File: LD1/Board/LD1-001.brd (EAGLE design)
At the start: 72 x 72 mm, 13 parts, among them IC1 TLC5941NT, IC2 TLC5941NT, IC3 TLC5941NT

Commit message: Before the first prototyping.
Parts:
- removed CN2, CN3: (no value), jst-ph:B16B-PH-K-S
- removed SV1: (no value), con-ml:ML10
- added C4: 0.01u, rcl:C025-025X050
- added IC4: TLC5941NT, adafruit:DIL28-3
- added JP1, JP2, JP3, JP4: (no value), pinhead:2X16
- added JP5: (no value), pinhead:1X02
- added R4: 4.7k, resistor:0204/5
- CN1: device jst-ph:B16B-PH-K-S -> jst-ph:S8B-PH-K-S
- moved C1 39.8 mm to (53.3, 15.2), turned to 90 degrees
- moved R1 38.1 mm to (53.3, 21.6), turned to 90 degrees
- moved IC1 32.5 mm to (31.8, 19.1), turned to 0 degrees
- moved CN1 30.0 mm to (8.00, 17.0), turned to 90 degrees
- moved C2 17.8 mm to (15.2, 27.9)
- moved C3 15.3 mm to (35.6, 27.9)
- moved IC2 14.2 mm to (19.1, 49.5)
- moved R2 12.5 mm to (21.6, 27.9)
- moved IC3 11.7 mm to (39.4, 49.5)
- moved R3 10.2 mm to (41.9, 27.9)
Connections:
- removed net LED2B: CN3.6, IC3.5
- removed net LED2G: CN3.5, IC3.4
- removed net LED3B: CN3.9, IC3.8
- removed net LED3G: CN3.8, IC3.7
- removed net LED3R: CN3.7, IC3.6
- removed net LEDA: CN3.1, IC3.28
- removed net SIN: IC3.26, SV1.3
- new net N$37: IC4.20, R4.2
- new net N$48: IC3.8, JP3.17
- new net N$49: IC3.9, JP3.19
- new net N$50: IC3.10, JP3.21
- new net N$51: IC3.11, JP3.23
- new net N$52: IC3.12, JP3.25
- new net N$53: IC3.13, JP3.27
- new net N$54: IC3.14, JP3.29
- new net N$55: IC3.15, JP3.31
- new net N$56: IC4.28, JP4.1
- new net N$57: IC4.1, JP4.3
- new net N$58: IC4.2, JP4.5
- new net N$59: IC4.3, JP4.7
- new net N$60: IC4.4, JP4.9
- new net N$61: IC4.5, JP4.11
- new net N$62: IC4.6, JP4.13
- new net N$63: IC4.7, JP4.15
- new net N$64: IC4.8, JP4.17
- new net N$66: IC4.9, JP4.19
- new net N$67: IC4.10, JP4.21
- new net N$68: IC4.11, JP4.23
- new net N$69: IC4.12, JP4.25
- new net N$70: IC4.13, JP4.27
- new net N$71: IC4.14, JP4.29
- new net N$72: IC4.15, JP4.31
- new net N$73: JP1.10, JP1.12, JP1.14, JP1.16, JP1.18, JP1.2, JP1.20, JP1.22, JP1.24, JP1.26, JP1.28, JP1.30, JP1.32, JP1.4, JP1.6, JP1.8, JP2.10, JP2.12, JP2.14, JP2.16, JP2.18, JP2.2, JP2.20, JP2.22, JP2.24, JP2.26, JP2.28, JP2.30, JP2.32, JP2.4, JP2.6, JP2.8, JP3.10, JP3.12, JP3.14, JP3.16, JP3.18, JP3.2, JP3.20, JP3.22, JP3.24, JP3.26, JP3.28, JP3.30, JP3.32, JP3.4, JP3.6, JP3.8, JP4.10, JP4.12, JP4.14, JP4.16, JP4.18, JP4.2, JP4.20, JP4.22, JP4.24, JP4.26, JP4.28, JP4.30, JP4.32, JP4.4, JP4.6, JP4.8, JP5.1
- net BLANK: now also CN1.3, IC4.23; no longer SV1.5
- net GND: now also C4.2, CN1.2, IC4.22, JP5.2; no longer SV1.10, SV1.2
- net GSCLCK: now also CN1.4, IC4.18; no longer SV1.7
- net MODE: now also CN1.8, IC4.27; no longer SV1.8
- net N$1: now also CN1.6, IC1.26; no longer CN2.16, IC2.15
- net N$10: now also IC1.5, JP1.11; no longer IC2.26, IC3.17
- net N$11: now also IC1.6, JP1.13; no longer CN2.4, IC2.3
- net N$12: now also IC1.7, JP1.15; no longer CN3.2, IC3.1
- net N$13: now also IC1.8, JP1.17; no longer CN2.5, IC2.4
- net N$14: now also IC1.9, JP1.19; no longer CN3.3, IC3.2
- net N$15: now also IC1.10, JP1.21; no longer CN2.6, IC2.5
- net N$16: now also IC1.11, JP1.23; no longer CN2.7, IC2.6
- net N$17: now also IC1.12, JP1.25; no longer CN2.8, IC2.7
- net N$18: now also IC1.13, JP1.27; no longer CN2.9, IC2.8
- net N$19: now also IC1.14, JP1.29; no longer CN2.10, IC2.9
- net N$2: now also IC1.17, IC2.26; no longer CN2.2, IC2.1
- net N$20: now also IC1.15, JP1.31; no longer CN2.11, IC2.10
- net N$21: now also IC2.28, JP2.1; no longer CN2.12, IC2.11
- net N$22: now also IC2.1, JP2.3; no longer CN2.13, IC2.12
- net N$23: now also IC2.2, JP2.5; no longer CN2.14, IC2.13
- net N$24: now also IC2.3, JP2.7; no longer CN3.15, IC3.14
- net N$25: now also IC2.4, JP2.9; no longer CN3.16, IC3.15
- net N$26: now also IC2.5, JP2.11; no longer CN2.15, IC2.14
- net N$27: now also IC2.6, JP2.13; no longer CN2.1, IC2.28
- net N$28: now also IC2.7, JP2.15; no longer CN1.16, IC1.15
- net N$29: now also IC2.8, JP2.17; no longer CN1.15, IC1.14
- net N$3: now also IC2.17, IC3.26; no longer CN3.13, IC3.12
- net N$30: now also IC2.9, JP2.19; no longer CN1.14, IC1.13
- net N$31: now also IC2.10, JP2.21; no longer CN1.13, IC1.12
- net N$32: now also IC2.11, JP2.23; no longer CN1.12, IC1.11
- net N$33: now also IC2.12, JP2.25; no longer CN1.11, IC1.10
- net N$34: now also IC2.13, JP2.27; no longer CN1.10, IC1.9
- net N$35: now also IC2.14, JP2.29; no longer CN1.9, IC1.8
- net N$36: now also IC2.15, JP2.31; no longer CN1.8, IC1.7
- net N$38: now also IC3.28, JP3.1; no longer CN1.7, IC1.6
- net N$39: now also IC3.1, JP3.3; no longer CN1.6, IC1.5
- net N$4: now also IC3.17, IC4.26; no longer CN2.3, IC2.2
- net N$40: now also IC3.2, JP3.5; no longer CN1.5, IC1.4
- net N$41: now also IC3.3, JP3.7; no longer CN1.4, IC1.3
- net N$42: now also IC3.4, JP3.9; no longer CN1.3, IC1.2
- net N$43: now also IC3.5, JP3.11; no longer CN1.2, IC1.1
- net N$44: now also IC3.6, JP3.13; no longer CN1.1, IC1.28
- net N$45: now also IC3.7, JP3.15; no longer IC1.26, IC2.17
- net N$5: now also IC1.28, JP1.1; no longer CN3.14, IC3.13
- net N$6: now also IC1.1, JP1.3; no longer CN3.10, IC3.9
- net N$7: now also IC1.2, JP1.5; no longer CN3.11, IC3.10
- net N$8: now also IC1.3, JP1.7; no longer CN3.12, IC3.11
- net N$9: now also IC1.4, JP1.9; no longer CN3.4, IC3.3
- net SCLCK: now also CN1.7, IC4.25; no longer SV1.4
- net VCC: now also C4.1, CN1.1, IC4.19, IC4.21, R4.1; no longer SV1.1
- net XLAT: now also CN1.5, IC4.24; no longer SV1.6
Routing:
- net N$73: track 0.00 -> 271.1 mm
- net SCLCK: track 70.1 -> 152.9 mm
- net MODE: track 58.3 -> 120.3 mm
- net N$2: track 6.73 -> 62.2 mm
- net N$10: track 62.4 -> 8.68 mm
- net GSCLCK: track 79.4 -> 125.3 mm
- net GND: track 145.5 -> 186.8 mm, vias 0 -> 1
- net N$45: track 48.9 -> 8.67 mm
- net N$3: track 5.99 -> 38.8 mm
- net N$4: track 6.46 -> 38.8 mm
- net N$37: track 0.00 -> 18.6 mm
- net N$55: track 0.00 -> 18.3 mm
- net N$72: track 0.00 -> 17.3 mm
- net N$56: track 0.00 -> 16.2 mm
- net BLANK: track 105.9 -> 119.9 mm, vias 1 -> 0
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
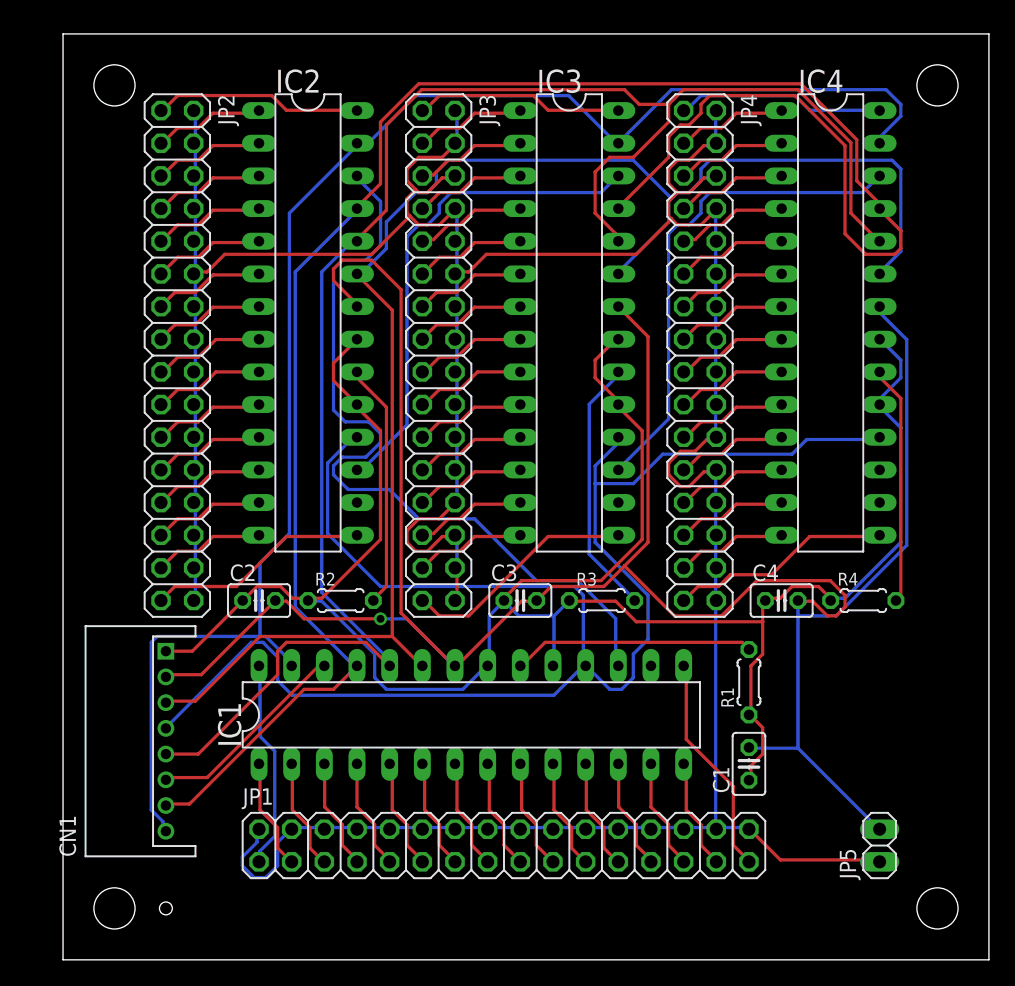
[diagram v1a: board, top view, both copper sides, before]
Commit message: Changed the positions of holes.
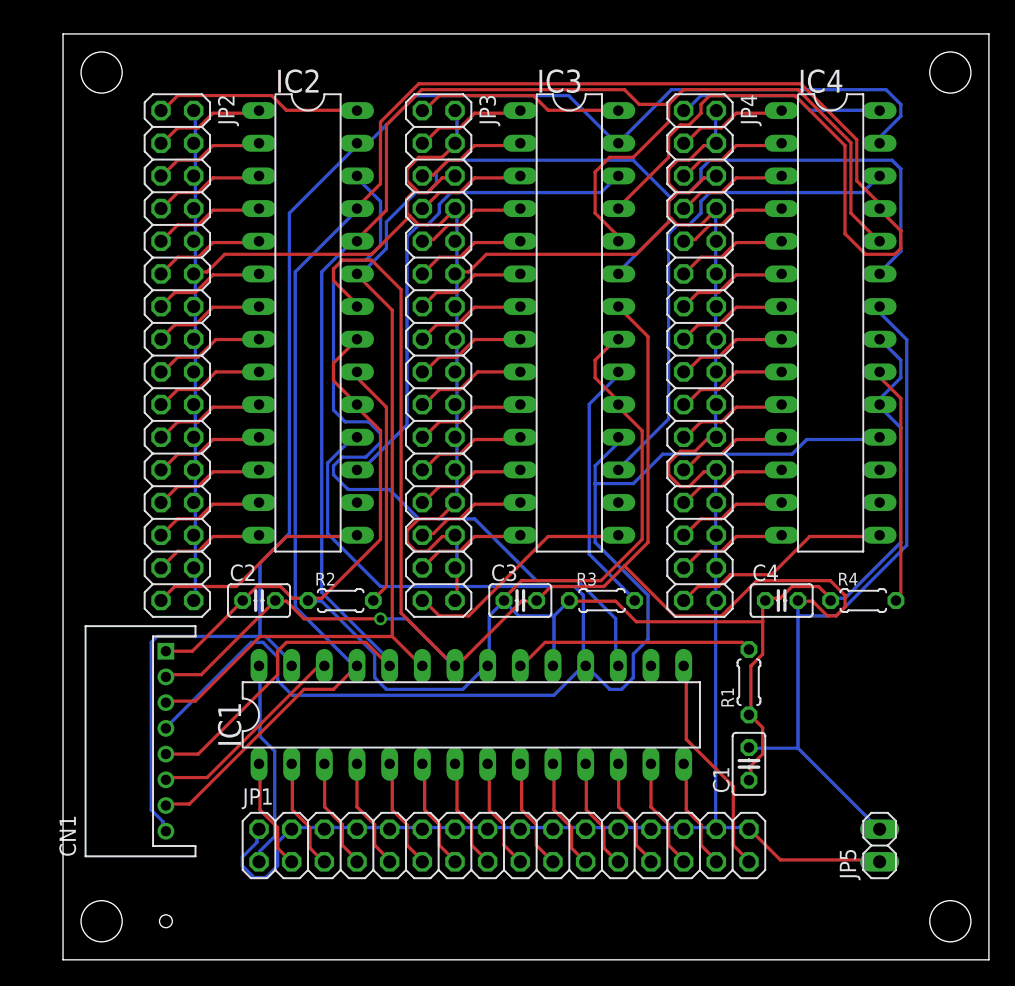
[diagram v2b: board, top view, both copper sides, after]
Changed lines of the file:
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@@
 <dimension x1="0" y1="0" x2="0" y2="72" x3="-2" y3="36" textsize="1.778" layer="20"/>
 <dimension x1="0" y1="0" x2="72" y2="0" x3="36" y3="-2" textsize="1.778" layer="20"/>
-<hole x="4" y="4" drill="3.2"/>
-<hole x="4" y="68" drill="3.2"/>
-<hole x="68" y="68" drill="3.2"/>
-<hole x="68" y="4" drill="3.2"/>
-<hole x="8" y="4" drill="1"/>
+<hole x="3" y="3" drill="3.2"/>
+<hole x="3" y="69" drill="3.2"/>
+<hole x="69" y="69" drill="3.2"/>
+<hole x="69" y="3" drill="3.2"/>
+<hole x="8" y="3" drill="1"/>
 </plain>
 <attributes>

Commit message: Removed D2 and D7.
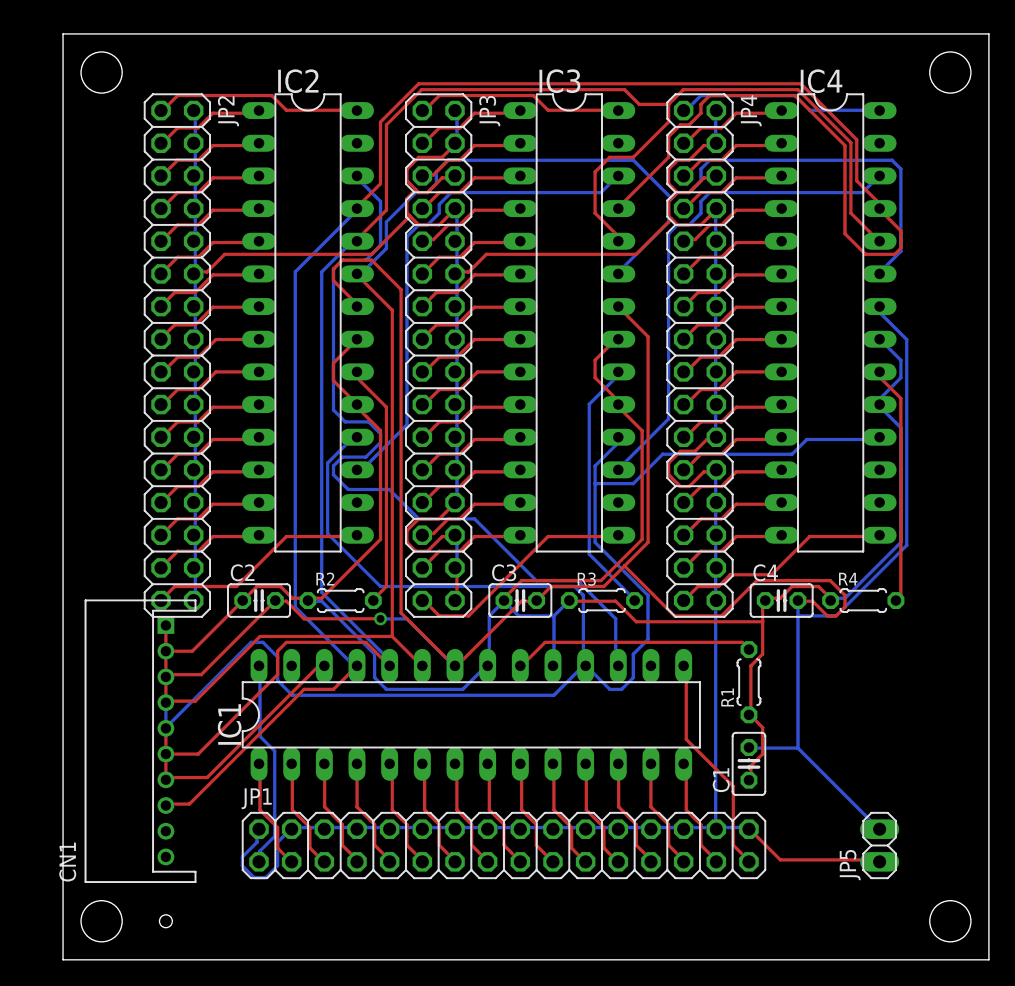
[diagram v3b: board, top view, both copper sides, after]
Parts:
- CN1: device jst-ph:S8B-PH-K-S -> jst-ph:S10B-PH-K-S
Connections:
- removed net MODE: CN1.8, IC1.27, IC2.27, IC3.27, IC4.27
- net GND: now also IC1.27, IC2.27, IC3.27, IC4.27
- net SCLCK: now also CN1.8; no longer CN1.7
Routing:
- net MODE: track 120.3 -> 0.00 mm
- net XLAT: track 132.8 -> 134.8 mm
- net VCC: track 166.8 -> 168.8 mm
- net GSCLCK: track 125.3 -> 127.2 mm
- net BLANK: track 119.9 -> 121.6 mm
- net N$1: track 16.1 -> 17.7 mm
- net GND: track 186.8 -> 188.1 mm
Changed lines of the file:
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@@
 <element name="IC1" library="adafruit" package="DIL28-3" value="TLC5941NT" x="31.75" y="19.05"/>
 <element name="R1" library="resistor" package="0204/5" value="4.7k" x="53.34" y="21.59" rot="R90"/>
-<element name="CN1" library="jst-ph" package="S8B-PH-K-S" value="" x="8" y="17" rot="R90"/>
+<element name="CN1" library="jst-ph" package="S10B-PH-K-S" value="" x="8" y="17" rot="R90"/>
 <element name="C4" library="rcl" package="C025-025X050" value="0.01u" x="55.88" y="27.94"/>
 <element name="JP1" library="pinhead" package="2X16" value="" x="34.29" y="8.89"/>
@@
 <contactref element="C3" pad="2"/>
 <contactref element="IC2" pad="22"/>
-<contactref element="IC3" pad="22"/>
-<contactref element="IC1" pad="22"/>
 <contactref element="CN1" pad="2"/>
 <contactref element="C4" pad="2"/>
@@
 <wire x1="10.7442" y1="22.1742" x2="8.001" y2="22.1742" width="0.254" layer="1"/>
 <wire x1="16.51" y1="27.94" x2="10.7442" y2="22.1742" width="0.254" layer="1"/>
-<wire x1="8.001" y1="22.1742" x2="8" y2="22" width="0.254" layer="1"/>
+<wire x1="8.001" y1="22.1742" x2="8" y2="24" width="0.254" layer="1"/>
 <wire x1="35.6616" y1="27.8892" x2="30.6324" y2="22.86" width="0.254" layer="1"/>
 <wire x1="36.8046" y1="27.8892" x2="35.6616" y2="27.8892" width="0.254" layer="1"/>
-<wire x1="30.6324" y1="22.86" x2="30.48" y2="22.86" width="0.254" layer="1"/>
 <wire x1="36.8046" y1="27.8892" x2="36.83" y2="27.94" width="0.254" layer="1"/>
 <wire x1="21.0312" y1="52.8066" x2="22.86" y2="50.9778" width="0.254" layer="1"/>
@@
 <wire x1="30.4038" y1="22.86" x2="26.289" y2="26.9748" width="0.254" layer="1"/>
 <wire x1="22.86" y1="50.9778" x2="22.86" y2="50.8" width="0.254" layer="1"/>
-<wire x1="30.4038" y1="22.86" x2="30.48" y2="22.86" width="0.254" layer="1"/>
 <wire x1="45.4914" y1="48.4632" x2="43.2054" y2="50.7492" width="0.254" layer="1"/>
 <wire x1="45.4914" y1="32.4612" x2="45.4914" y2="48.4632" width="0.254" layer="1"/>
@@
 <wire x1="37.9476" y1="29.0322" x2="42.0624" y2="29.0322" width="0.254" layer="1"/>
 <wire x1="37.0332" y1="28.1178" x2="37.9476" y2="29.0322" width="0.254" layer="1"/>
-<wire x1="43.2054" y1="50.7492" x2="43.18" y2="50.8" width="0.254" layer="1"/>
 <wire x1="37.0332" y1="28.1178" x2="36.83" y2="27.94" width="0.254" layer="1"/>
 <wire x1="17.3736" y1="27.8892" x2="16.6878" y2="27.8892" width="0.254" layer="1"/>
@@
 <wire x1="30.4038" y1="22.86" x2="26.7462" y2="26.5176" width="0.254" layer="16"/>
 <wire x1="16.6878" y1="27.8892" x2="16.51" y2="27.94" width="0.254" layer="1"/>
-<wire x1="30.4038" y1="22.86" x2="30.48" y2="22.86" width="0.254" layer="16"/>
 <wire x1="58.293" y1="27.8892" x2="57.15" y2="27.8892" width="0.254" layer="1"/>
 <wire x1="59.436" y1="26.7462" x2="58.293" y2="27.8892" width="0.254" layer="1"/>
@@
 <wire x1="57.15" y1="27.8892" x2="57.15" y2="27.94" width="0.254" layer="1"/>
 <via x="24.6888" y="26.5176" extent="1-16" drill="0.6096"/>
+<contactref element="IC1" pad="22"/>
+<contactref element="IC3" pad="27"/>
+<contactref element="IC2" pad="27"/>
+<contactref element="IC4" pad="27"/>
+<contactref element="IC1" pad="27"/>
+<contactref element="IC3" pad="22"/>
+<wire x1="63.5" y1="50.8" x2="63.5" y2="63.5" width="0" layer="19" extent="1-1"/>
+<wire x1="43.18" y1="50.8" x2="43.2054" y2="50.7492" width="0" layer="19" extent="1-1"/>
+<wire x1="30.48" y1="22.86" x2="30.6324" y2="22.86" width="0" layer="19" extent="1-1"/>
+<wire x1="30.4038" y1="22.86" x2="30.48" y2="22.86" width="0" layer="19" extent="1-1"/>
+<wire x1="30.4038" y1="22.86" x2="30.4038" y2="22.86" width="0" layer="19" extent="1-16"/>
+<wire x1="17.78" y1="22.86" x2="18.7452" y2="26.5176" width="0" layer="19" extent="1-1"/>
+<wire x1="22.86" y1="63.5" x2="21.717" y2="54.4068" width="0" layer="19" extent="1-1"/>
+<wire x1="43.18" y1="63.5" x2="43.18" y2="50.8" width="0" layer="19" extent="1-1"/>
 </signal>
 <signal name="VCC">
@@
 <wire x1="10.0584" y1="24.003" x2="8.001" y2="24.003" width="0.254" layer="1"/>
 <wire x1="13.9446" y1="27.8892" x2="10.0584" y2="24.003" width="0.254" layer="1"/>
-<wire x1="8.001" y1="24.003" x2="8" y2="24" width="0.254" layer="1"/>
+<wire x1="8.001" y1="24.003" x2="8" y2="26" width="0.254" layer="1"/>
 <wire x1="13.9446" y1="27.8892" x2="13.97" y2="27.94" width="0.254" layer="1"/>
 <wire x1="17.8308" y1="28.1178" x2="18.9738" y2="28.1178" width="0.254" layer="1"/>
@@
 <wire x1="23.5458" y1="24.6888" x2="17.3736" y2="24.6888" width="0.254" layer="1"/>
 <wire x1="25.3746" y1="22.86" x2="23.5458" y2="24.6888" width="0.254" layer="1"/>
-<wire x1="8.001" y1="16.002" x2="8" y2="16" width="0.254" layer="1"/>
+<wire x1="8.001" y1="16.002" x2="8" y2="18" width="0.254" layer="1"/>
 <wire x1="25.3746" y1="22.86" x2="25.4" y2="22.86" width="0.254" layer="1"/>
 <wire x1="22.4028" y1="55.7784" x2="22.86" y2="55.7784" width="0.254" layer="16"/>
@@
 <wire x1="22.86" y1="56.007" x2="25.146" y2="58.293" width="0.254" layer="1"/>
 <wire x1="22.86" y1="56.007" x2="22.86" y2="55.88" width="0.254" layer="1"/>
-</signal>
-<signal name="MODE">
-<contactref element="IC4" pad="27"/>
-<contactref element="IC3" pad="27"/>
-<contactref element="IC2" pad="27"/>
-<contactref element="IC1" pad="27"/>
-<contactref element="CN1" pad="8"/>
-<wire x1="7.7724" y1="10.7442" x2="7.7724" y2="10.0584" width="0.254" layer="16"/>
-<wire x1="6.858" y1="11.6586" x2="7.7724" y2="10.7442" width="0.254" layer="16"/>
-<wire x1="6.858" y1="24.6888" x2="6.858" y2="11.6586" width="0.254" layer="16"/>
-<wire x1="7.3152" y1="25.146" x2="6.858" y2="24.6888" width="0.254" layer="16"/>
-<wire x1="15.7734" y1="25.146" x2="15.3162" y2="25.146" width="0.254" layer="16"/>
-<wire x1="15.3162" y1="25.146" x2="7.3152" y2="25.146" width="0.254" layer="16"/>
-<wire x1="17.6022" y1="23.3172" x2="15.7734" y2="25.146" width="0.254" layer="16"/>
-<wire x1="17.6022" y1="22.86" x2="17.6022" y2="23.3172" width="0.254" layer="16"/>
-<wire x1="7.7724" y1="10.0584" x2="8" y2="10" width="0.254" layer="16"/>
-<wire x1="17.6022" y1="22.86" x2="17.78" y2="22.86" width="0.254" layer="16"/>
-<wire x1="23.7744" y1="63.5508" x2="22.86" y2="63.5508" width="0.254" layer="16"/>
-<wire x1="27.432" y1="67.2084" x2="23.7744" y2="63.5508" width="0.254" layer="16"/>
-<wire x1="39.3192" y1="67.2084" x2="27.432" y2="67.2084" width="0.254" layer="16"/>
-<wire x1="42.9768" y1="63.5508" x2="39.3192" y2="67.2084" width="0.254" layer="16"/>
-<wire x1="22.86" y1="63.5508" x2="22.86" y2="63.5" width="0.254" layer="16"/>
-<wire x1="42.9768" y1="63.5508" x2="43.18" y2="63.5" width="0.254" layer="16"/>
-<wire x1="63.5508" y1="64.008" x2="63.5508" y2="63.5508" width="0.254" layer="16"/>
-<wire x1="65.151" y1="65.6082" x2="63.5508" y2="64.008" width="0.254" layer="16"/>
-<wire x1="65.151" y1="66.5226" x2="65.151" y2="65.6082" width="0.254" layer="16"/>
-<wire x1="64.008" y1="67.6656" x2="65.151" y2="66.5226" width="0.254" layer="16"/>
-<wire x1="47.3202" y1="67.6656" x2="64.008" y2="67.6656" width="0.254" layer="16"/>
-<wire x1="43.2054" y1="63.5508" x2="47.3202" y2="67.6656" width="0.254" layer="16"/>
-<wire x1="63.5508" y1="63.5508" x2="63.5" y2="63.5" width="0.254" layer="16"/>
-<wire x1="43.2054" y1="63.5508" x2="43.18" y2="63.5" width="0.254" layer="16"/>
-<wire x1="15.3162" y1="30.861" x2="15.3162" y2="25.146" width="0.254" layer="16"/>
-<wire x1="17.6022" y1="33.147" x2="15.3162" y2="30.861" width="0.254" layer="16"/>
-<wire x1="17.6022" y1="58.0644" x2="17.6022" y2="33.147" width="0.254" layer="16"/>
-<wire x1="22.86" y1="63.3222" x2="17.6022" y2="58.0644" width="0.254" layer="16"/>
-<wire x1="22.86" y1="63.3222" x2="22.86" y2="63.5" width="0.254" layer="16"/>
 </signal>
 <signal name="BLANK">
@@
 <wire x1="25.6032" y1="25.146" x2="15.3162" y2="25.146" width="0.254" layer="1"/>
 <wire x1="27.8892" y1="22.86" x2="25.6032" y2="25.146" width="0.254" layer="1"/>
-<wire x1="8.001" y1="20.1168" x2="8" y2="20" width="0.254" layer="1"/>
+<wire x1="8.001" y1="20.1168" x2="8" y2="22" width="0.254" layer="1"/>
 <wire x1="27.8892" y1="22.86" x2="27.94" y2="22.86" width="0.254" layer="1"/>
 <wire x1="25.6032" y1="50.5206" x2="22.86" y2="53.2638" width="0.254" layer="1"/>
@@
 <contactref element="IC2" pad="25"/>
 <contactref element="IC1" pad="25"/>
-<contactref element="CN1" pad="7"/>
 <wire x1="47.0916" y1="62.4078" x2="43.2054" y2="58.5216" width="0.254" layer="1"/>
 <wire x1="47.0916" y1="64.008" x2="47.0916" y2="62.4078" width="0.254" layer="1"/>
@@
 <wire x1="21.0312" y1="21.0312" x2="18.7452" y2="21.0312" width="0.254" layer="1"/>
 <wire x1="22.86" y1="22.86" x2="21.0312" y2="21.0312" width="0.254" layer="1"/>
-<wire x1="8.001" y1="12.1158" x2="8" y2="12" width="0.254" layer="1"/>
 <wire x1="18.0594" y1="53.4924" x2="22.86" y2="58.293" width="0.254" layer="16"/>
 <wire x1="18.0594" y1="27.432" x2="18.0594" y2="53.4924" width="0.254" layer="16"/>
@@
 <wire x1="63.3222" y1="58.5216" x2="63.5" y2="58.42" width="0.254" layer="1"/>
 <wire x1="22.86" y1="58.5216" x2="22.86" y2="58.42" width="0.254" layer="1"/>
+<contactref element="CN1" pad="8"/>
+<wire x1="8" y1="12" x2="8.001" y2="12.1158" width="0" layer="19" extent="1-1"/>
 </signal>
 <signal name="N$37">
@@
 <wire x1="38.1762" y1="20.574" x2="17.8308" y2="20.574" width="0.254" layer="16"/>
 <wire x1="40.4622" y1="22.86" x2="38.1762" y2="20.574" width="0.254" layer="16"/>
-<wire x1="8.001" y1="18.0594" x2="8" y2="18" width="0.254" layer="16"/>
+<wire x1="8.001" y1="18.0594" x2="8" y2="20" width="0.254" layer="16"/>
 <wire x1="22.4028" y1="40.4622" x2="22.86" y2="40.4622" width="0.254" layer="16"/>
 <wire x1="20.574" y1="38.6334" x2="22.4028" y2="40.4622" width="0.254" layer="16"/>
@@
 <wire x1="19.8882" y1="22.86" x2="11.2014" y2="14.1732" width="0.254" layer="1"/>
 <wire x1="20.32" y1="22.86" x2="19.8882" y2="22.86" width="0.254" layer="1"/>
-<wire x1="8.001" y1="14.1732" x2="8" y2="14" width="0.254" layer="1"/>
+<wire x1="8.001" y1="14.1732" x2="8" y2="16" width="0.254" layer="1"/>
 </signal>
 <signal name="N$2">
